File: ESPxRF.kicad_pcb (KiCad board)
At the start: 4 copper layers, 22 parts, among them J1 Conn_Coaxial, J2 USB_C_Receptacle_USB2.0, U1 ESP32-S3, U2 NRF24L01, U3 NCP115ASN330T2G, U4 USBLC6-2SC6

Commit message: nearly finished V1
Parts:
- added C10: 1p, Capacitor_SMD:C_0402_1005Metric_Pad0.74x0.62mm_HandSolder, F.Cu at (139.7, 64.7)
- added C11: 2n2, Capacitor_SMD:C_0402_1005Metric_Pad0.74x0.62mm_HandSolder, F.Cu at (142.1, 69.3)
- added C12: 4p7, Capacitor_SMD:C_0402_1005Metric_Pad0.74x0.62mm_HandSolder, F.Cu at (142.1, 68.1)
- added C13: 10u, Capacitor_SMD:C_0603_1608Metric_Pad1.08x0.95mm_HandSolder, F.Cu at (108.0, 62.3)
- added C14: 100n, Capacitor_SMD:C_0603_1608Metric_Pad1.08x0.95mm_HandSolder, F.Cu at (109.7, 62.3)
- added C15: 33n, Capacitor_SMD:C_0402_1005Metric_Pad0.74x0.62mm_HandSolder, F.Cu at (136.3, 79.0)
- added C16: 22p, Capacitor_SMD:C_0402_1005Metric_Pad0.74x0.62mm_HandSolder, F.Cu at (144.7, 73.7)
- added C17: 22p, Capacitor_SMD:C_0402_1005Metric_Pad0.74x0.62mm_HandSolder, F.Cu at (144.9, 78.1)
- added L1: 100R @ 100MHz, Inductor_SMD:L_0603_1608Metric_Pad1.05x0.95mm_HandSolder, F.Cu at (108.9, 64.8)
- added L2: 3n9, Inductor_SMD:L_0402_1005Metric_Pad0.77x0.64mm_HandSolder, F.Cu at (139.1, 68.7)
- added L3: 8n2, Inductor_SMD:L_0402_1005Metric_Pad0.77x0.64mm_HandSolder, F.Cu at (139.7, 70.4)
- added L4: 2n7, Inductor_SMD:L_0402_1005Metric_Pad0.77x0.64mm_HandSolder, F.Cu at (140.3, 68.7)
- added R5: 22k, Resistor_SMD:R_0402_1005Metric_Pad0.72x0.64mm_HandSolder, F.Cu at (135.7, 75.0)
- added R6: 1M, Resistor_SMD:R_0402_1005Metric_Pad0.72x0.64mm_HandSolder, F.Cu at (142.9, 75.9)
- added Y1: Crystal_GND24_Small, Crystal:Crystal_SMD_2520-4Pin_2.5x2.0mm, F.Cu at (145.6, 75.7)
- C2, C3, C4: value 10u -> 100n; footprint Capacitor_SMD:C_0603_1608Metric_Pad1.08x0.95mm_HandSolder -> Capacitor_SMD:C_0402_1005Metric_Pad0.74x0.62mm_HandSolder
- C5, C6: value 100n -> 10u
- C9: value 100n -> 1p5; footprint Capacitor_SMD:C_0603_1608Metric_Pad1.08x0.95mm_HandSolder -> Capacitor_SMD:C_0402_1005Metric_Pad0.74x0.62mm_HandSolder
- F1: value 100mA -> 500mA
- J1: value Conn_Coaxial -> USB_C_Receptacle_USB2.0; footprint Connector_Coaxial:SMA_Amphenol_132289_EdgeMount -> Connector_USB:USB_C_Receptacle_GCT_USB4105-xx-A_16P_TopMnt_Horizontal
- J2: value USB_C_Receptacle_USB2.0 -> ANT; footprint Connector_USB:USB_C_Receptacle_GCT_USB4105-xx-A_16P_TopMnt_Horizontal -> Connector_Coaxial:SMA_Samtec_SMA-J-P-X-ST-EM1_EdgeMount
- R1, R2: value 5k1 -> 1k3
- R3, R4: value 1k3 -> 5k1
- U1: value ESP32-S3 -> NCP115ASN330T2G; footprint ESP32:XCVR_ESP32S3WROOM1N8R8 -> NCP115ASN330T2G:NCP115ASN330T2G
- U3: value NCP115ASN330T2G -> USBLC6-2SC6; footprint NCP115ASN330T2G:NCP115ASN330T2G -> SnapEda:SOT95P280X145-6N
- U4: value USBLC6-2SC6 -> ESP32-S3; footprint SnapEda:SOT95P280X145-6N -> ESP32:XCVR_ESP32S3WROOM1N8R8
- moved J1 75.7 mm to (90.0, 72.9), turned to -90 degrees
- moved J2 67.8 mm to (139.1, 61.5), turned to 180 degrees
- moved R4 43.7 mm to (93.1, 66.4)
- moved R3 42.2 mm to (93.1, 79.4)
- moved U4 39.1 mm to (121.0, 66.0)
- moved F1 36.9 mm to (96.8, 66.4)
- moved C5 30.3 mm to (99.3, 67.3), turned to -90 degrees
- moved U3 29.2 mm to (98.8, 72.4)
- moved D2 28.5 mm to (106.0, 72.4)
- moved D1 27.8 mm to (106.0, 70.8)
- moved R1 25.8 mm to (109.4, 70.8), turned to 180 degrees
- moved R2 25.7 mm to (109.4, 72.4), turned to 180 degrees
- moved C6 24.6 mm to (106.4, 67.3), turned to -90 degrees
- moved C7 23.6 mm to (108.0, 67.3), turned to -90 degrees
- moved C8 22.6 mm to (109.8, 67.3), turned to -90 degrees
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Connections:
- C1 pad 1: +5V -> +3V3
- C5 pad 1: +3V3 -> +5V
- C6 pad 1: +3V3 -> Net-(U1-out)
- C7 pad 1: +3V3 -> Net-(U1-out)
- C9 pad 1: GND -> Net-(C9-Pad1)
- C9 pad 2: Net-(J2-SHIELD) -> Net-(J2-In)
- R1 pad 1: Net-(J2-CC2) -> Net-(U4-IO16)
- R1 pad 2: GND -> Net-(D1-A)
- R2 pad 1: Net-(J2-CC1) -> Net-(U4-IO17)
- R2 pad 2: GND -> Net-(D2-A)
- R3 pad 1: unconnected-(R3-Pad1) -> Net-(J1-CC2)
- R3 pad 2: Net-(D1-A) -> GND
- R4 pad 1: unconnected-(R4-Pad1) -> Net-(J1-CC1)
- R4 pad 2: Net-(D2-A) -> GND
- U1 pad 1: GND -> +5V
- U1 pad 2: +3V3 -> GND
- U1 pad 3: unconnected-(U1-EN-Pad3) -> +5V
- U1 pad 4: unconnected-(U1-IO4-Pad4) -> (no net)
- U1 pad 5: unconnected-(U1-IO5-Pad5) -> Net-(U1-out)
- U2 pad 1: unconnected-(U2-CE-Pad1) -> CE
- U2 pad 10: unconnected-(U2-XC1-Pad10) -> XC1
- U2 pad 11: unconnected-(U2-VDD_PA-Pad11) -> VDD_PA
- U2 pad 12: unconnected-(U2-ANT1-Pad12) -> ANT1
- U2 pad 13: unconnected-(U2-ANT2-Pad13) -> ANT2
- U2 pad 16: unconnected-(U2-IREF-Pad16) -> Net-(U2-IREF)
- U2 pad 19: unconnected-(U2-DVDD-Pad19) -> Net-(U2-DVDD)
- U2 pad 2: unconnected-(U2-CSN-Pad2) -> CSN
- U2 pad 3: unconnected-(U2-SCK-Pad3) -> SCK
- U2 pad 4: unconnected-(U2-MOSI-Pad4) -> MOSI
- U2 pad 5: unconnected-(U2-MISO-Pad5) -> MISO
- U2 pad 6: unconnected-(U2-IRQ-Pad6) -> IRQ
- U2 pad 9: unconnected-(U2-XC2-Pad9) -> XC2
- U3 pad 1: +5V -> USBCON_D-
- U3 pad 3: +5V -> USBCON_D+
- U3 pad 4: (no net) -> USB_D+
- U3 pad 5: +3V3 -> +5V
- U4 pad 1: unconnected-(U4-Pad1) -> GND
- U4 pad 2: GND -> +3V3
- U4 pad 3: unconnected-(U4-Pad3) -> +3V3
- U4 pad 5: +5V -> unconnected-(U4-IO5-Pad5)
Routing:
- net GND: track 0.00 -> 102.8 mm, vias 0 -> 31
- net +3V3: track 0.00 -> 71.5 mm, vias 0 -> 5
- net CSN: track 0.00 -> 32.7 mm, vias 0 -> 2
- net MISO: track 0.00 -> 24.7 mm
- net MOSI: track 0.00 -> 22.4 mm
- net SCK: track 0.00 -> 19.8 mm
- net +5V: track 0.00 -> 15.7 mm
- net USB_D-: track 0.00 -> 14.4 mm
- net USB_D+: track 0.00 -> 14.4 mm
- net Net-(F1-Pad1): track 0.00 -> 13.0 mm, vias 0 -> 2
- net CE: track 0.00 -> 12.9 mm
- net VDD_PA: track 0.00 -> 8.64 mm
- net Net-(J1-CC1): track 0.00 -> 6.81 mm
- net Net-(J1-CC2): track 0.00 -> 6.33 mm
- net ANT2: track 0.00 -> 6.03 mm
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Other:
- board outline added: 62.6 x 23.8 mm
- board text added: "RX"
- board text added: "TX"

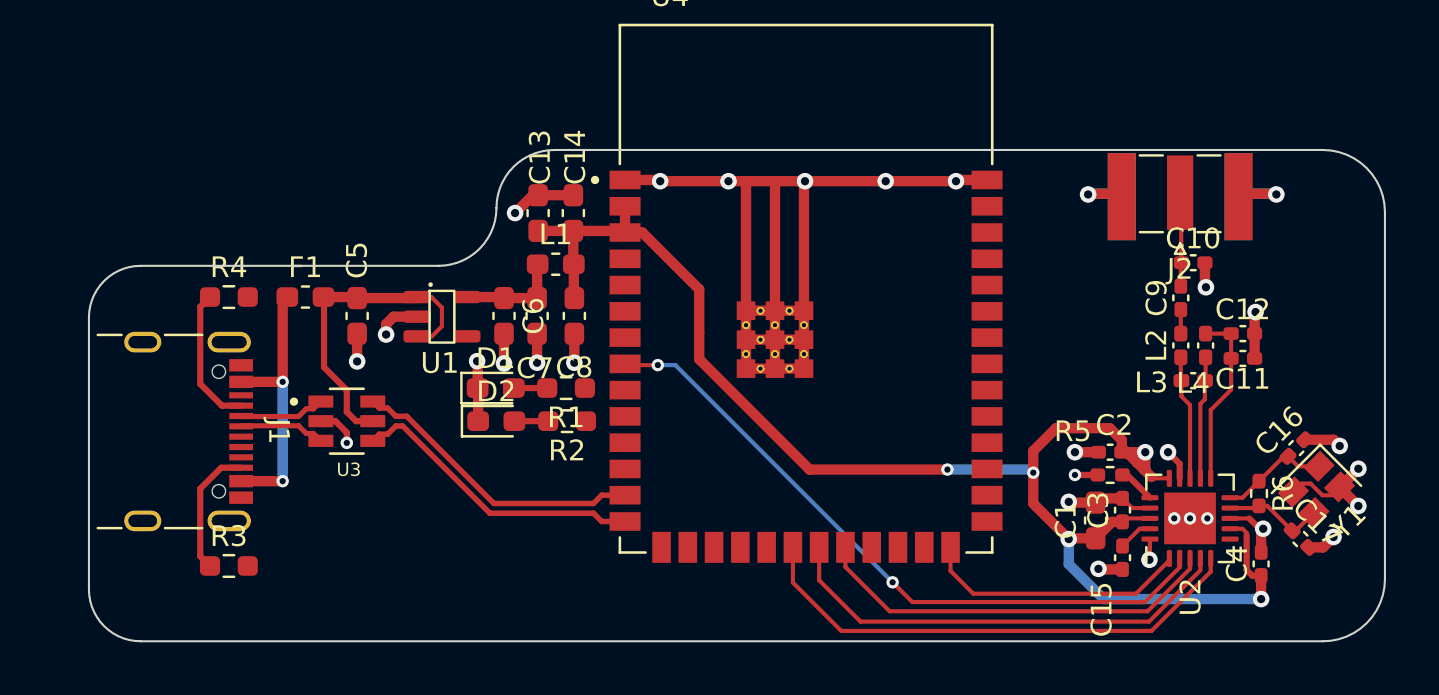
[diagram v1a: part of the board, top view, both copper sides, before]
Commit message: ground pour and optimizations
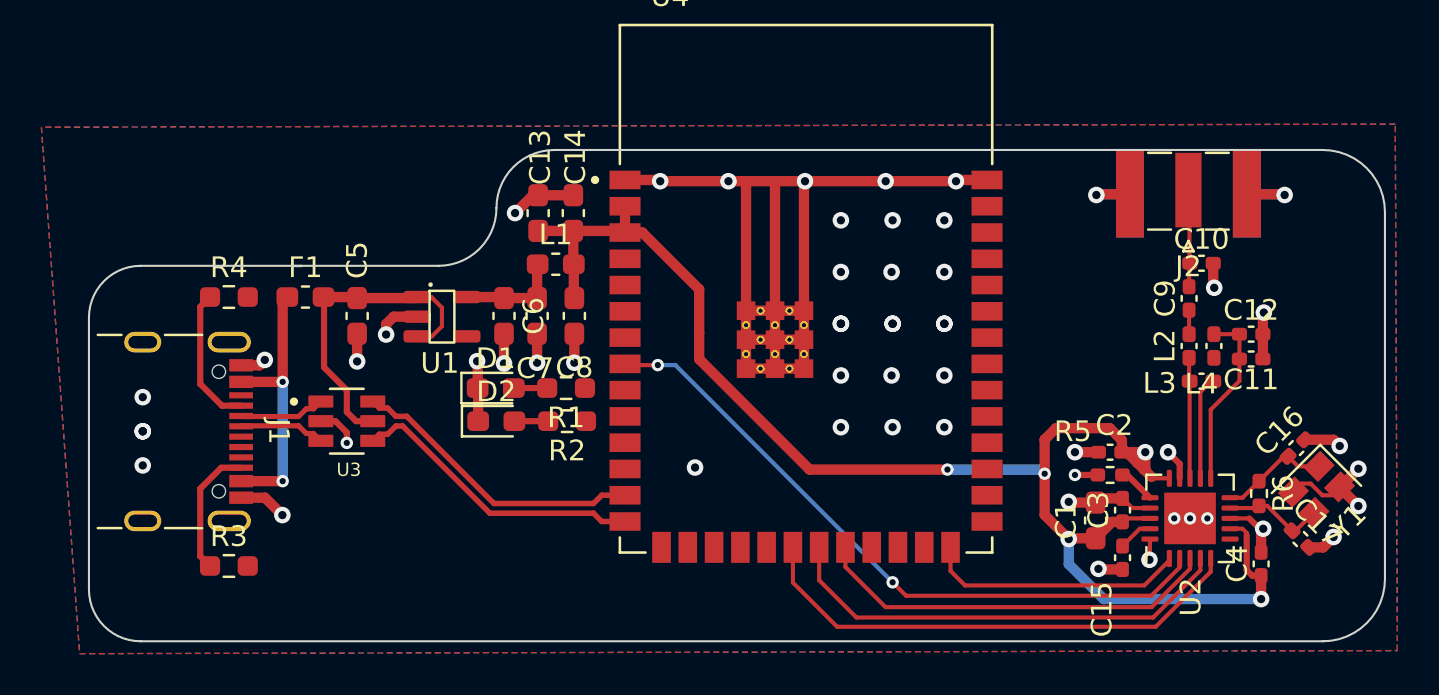
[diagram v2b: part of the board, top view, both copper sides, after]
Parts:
- moved J2 0.42 mm to (139.4, 61.4)
- moved C10 0.40 mm to (140.1, 64.7)
- moved L3 0.40 mm to (140.1, 70.4)
- moved L4 0.40 mm to (140.7, 68.7)
- moved C12 0.40 mm to (142.5, 68.2)
- moved C11 0.40 mm to (142.5, 69.4)
- moved C9 0.40 mm to (139.5, 66.4)
- moved L2 0.40 mm to (139.5, 68.7)
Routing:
- net GND: track 102.8 -> 106.4 mm, vias 31 -> 56
- net ANT1: track 5.96 -> 5.02 mm
- added copper zone on B.Cu, net GND
- added copper zone on F.Cu, net GND

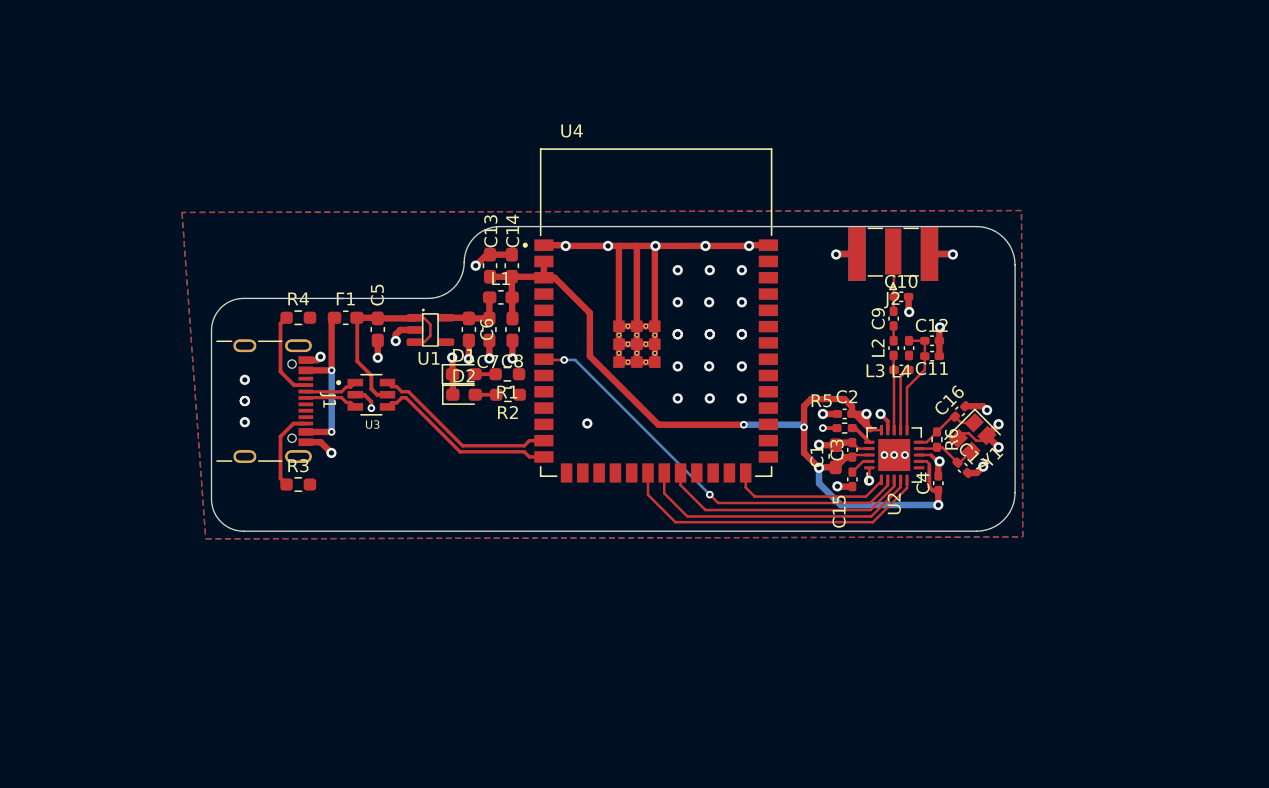
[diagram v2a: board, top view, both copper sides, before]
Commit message: added side mouting hole for I guess keyrings
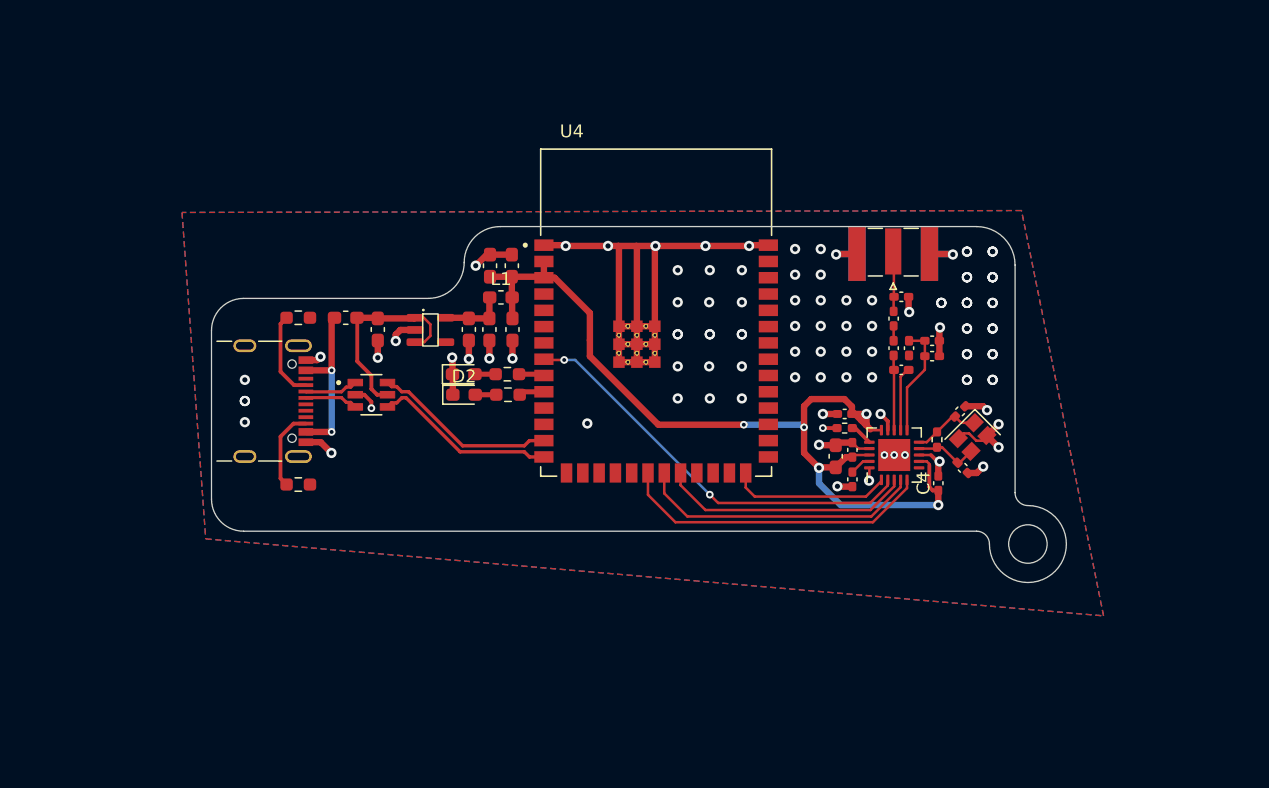
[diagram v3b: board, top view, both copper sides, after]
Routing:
- net Net-(U4-IO17): track 0.00 -> 1.98 mm
- net Net-(U4-IO16): track 0.00 -> 1.98 mm
- net GND: vias 56 -> 108
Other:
- board size 62.6 x 23.8 mm -> 66.6 x 27.7 mm
